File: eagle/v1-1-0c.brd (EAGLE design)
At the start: 313 x 132.9 mm, 179 parts, among them J1 CR22A-44D-2.54DSA(70), J3 26-60-4040, J4 AUDIO_JACK_3.5MM_PTH, J5 DIN5, SW1 3PDT-AQ-SWITCH, SW2 9077-1, U10 7805, U11 74LS10N, U13 74LS04N, U14 4528N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

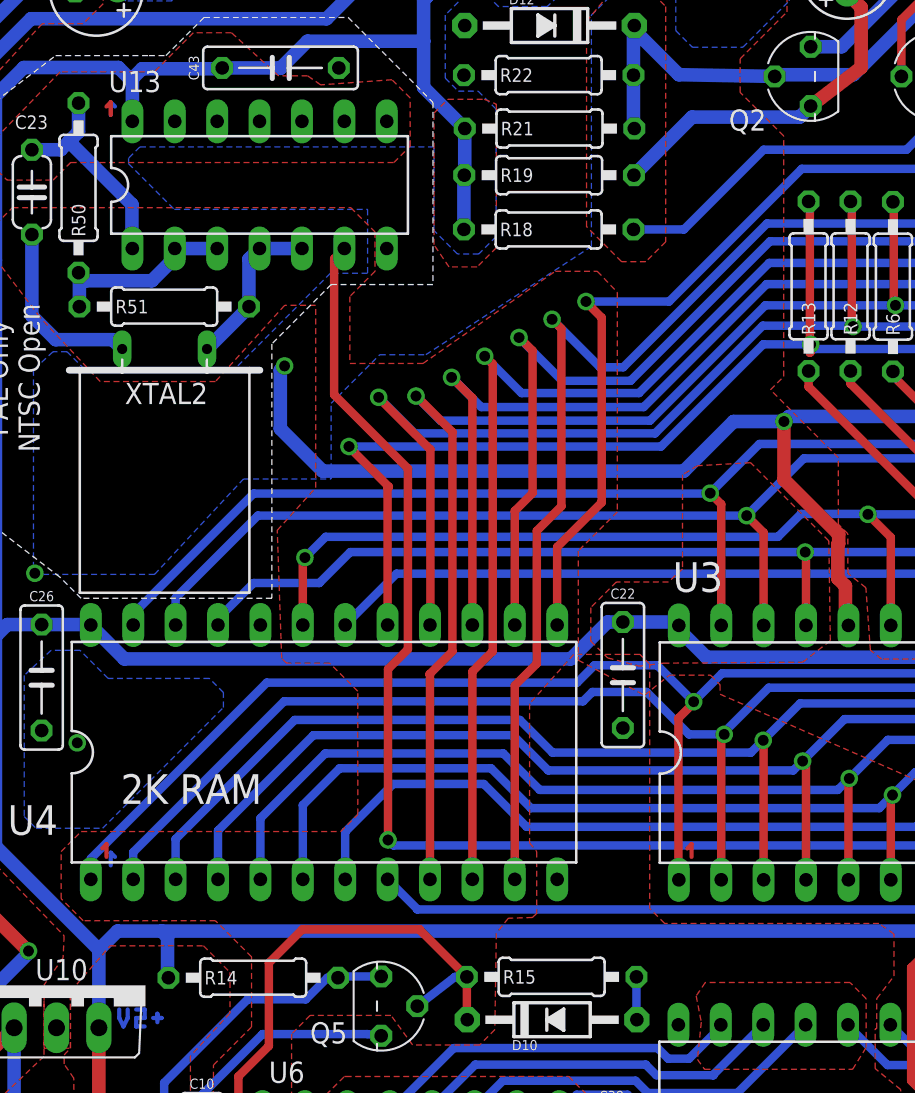
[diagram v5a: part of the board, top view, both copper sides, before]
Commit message: 19 OCT 2020 fixes from Errata
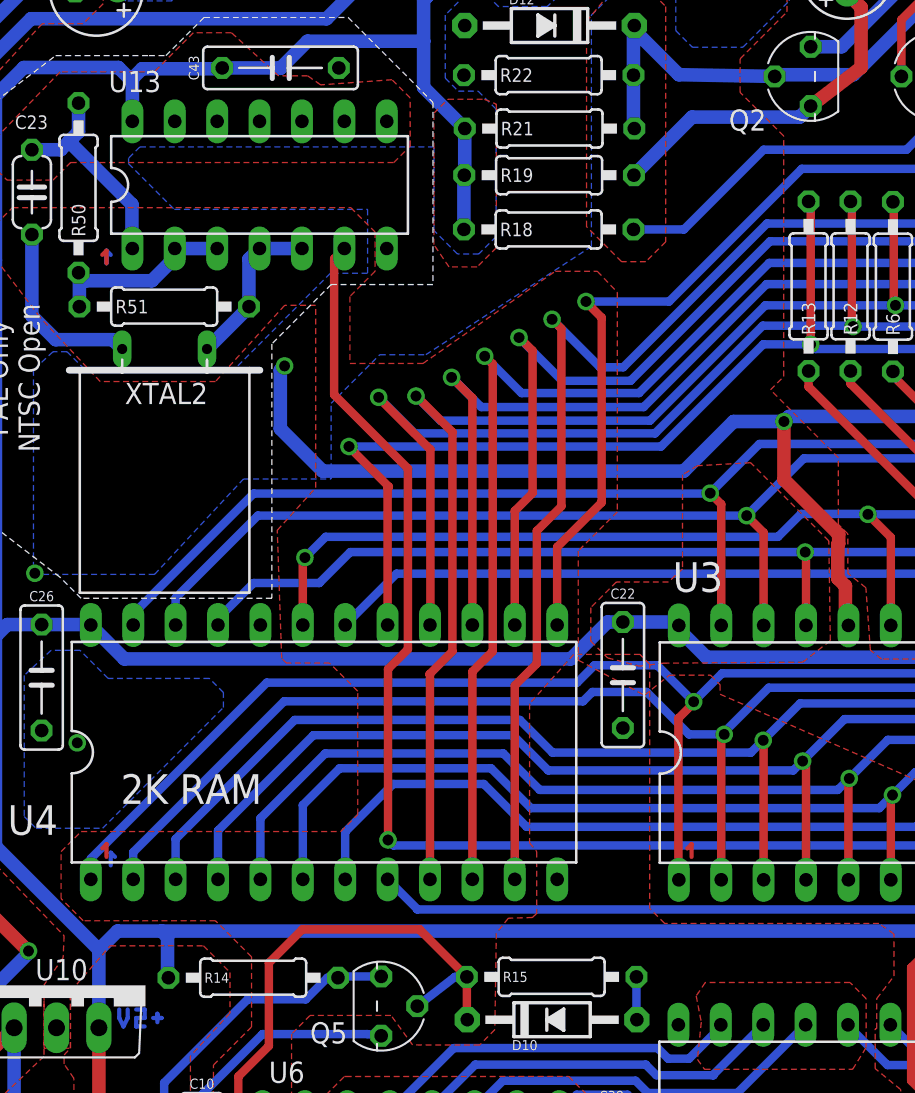
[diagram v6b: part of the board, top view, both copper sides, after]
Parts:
- C1: value 1uF @ 50v -> 1uF@50/10uF@16
- R14: value 2.2k -> 2.2k/680
- R15: value 1.2k -> 1.2k/2.2k
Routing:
- net CD07: track 106.2 -> 105.3 mm
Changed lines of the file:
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@@
 <grid distance="10" unitdist="mil" unit="mil" style="lines" multiple="1" display="no" altdistance="1" altunitdist="mil" altunit="mil"/>
 <layers>
-<layer number="1" name="Top" color="4" fill="1" visible="yes" active="yes"/>
+<layer number="1" name="Top" color="4" fill="1" visible="no" active="yes"/>
 <layer number="2" name="Route2" color="16" fill="1" visible="no" active="no"/>
 <layer number="3" name="Route3" color="17" fill="1" visible="no" active="no"/>
@@
 <layer number="14" name="Route14" color="22" fill="1" visible="no" active="no"/>
 <layer number="15" name="Route15" color="23" fill="1" visible="no" active="no"/>
-<layer number="16" name="Bottom" color="1" fill="1" visible="yes" active="yes"/>
+<layer number="16" name="Bottom" color="1" fill="1" visible="no" active="yes"/>
 <layer number="17" name="Pads" color="2" fill="1" visible="yes" active="yes"/>
 <layer number="18" name="Vias" color="2" fill="1" visible="yes" active="yes"/>
@@
 <layer number="46" name="Milling" color="3" fill="1" visible="yes" active="yes"/>
 <layer number="47" name="Measures" color="7" fill="1" visible="yes" active="yes"/>
-<layer number="48" name="Document" color="7" fill="1" visible="yes" active="yes"/>
+<layer number="48" name="Document" color="7" fill="1" visible="no" active="yes"/>
 <layer number="49" name="Reference" color="7" fill="1" visible="no" active="yes"/>
 <layer number="50" name="dxf" color="7" fill="1" visible="yes" active="yes"/>
@@
 <wire x1="9.599640625" y1="99.886" x2="11.58331875" y2="99.886" width="0.1524" layer="48"/>
 <wire x1="9.72361875" y1="89.49216875" x2="11.7073" y2="89.49216875" width="0.1524" layer="48"/>
-<wire x1="57.945209375" y1="75.54211875" x2="57.945209375" y2="62.39176875" width="0.1524" layer="48"/>
 <wire x1="56.9244" y1="74.606090625" x2="58.90808125" y2="74.606090625" width="0.1524" layer="48"/>
 <wire x1="57.04838125" y1="63.22148125" x2="59.032059375" y2="63.22148125" width="0.1524" layer="48"/>
@@
 <attribute name="VALUE" x="75.4888" y="72.1868" size="0.8128" layer="27" ratio="10" rot="R90" align="center-right"/>
 </element>
-<element name="R14" library="aq-rcl" package="0207/10" package3d_urn="urn:adsk.eagle:package:23491/2" value="2.2k" x="24.5364" y="27.813" smashed="yes">
-<attribute name="NAME" x="21.6154" y="27.813" size="0.8128" layer="25" ratio="10" align="center-left"/>
+<element name="R14" library="aq-rcl" package="0207/10" package3d_urn="urn:adsk.eagle:package:23491/2" value="2.2k/680" x="24.5364" y="27.813" smashed="yes">
+<attribute name="NAME" x="21.6154" y="27.813" size="0.6096" layer="25" ratio="10" align="center-left"/>
 <attribute name="POPULARITY" value="36" x="24.5364" y="27.813" size="1.778" layer="27" display="off"/>
 <attribute name="SPICEPREFIX" value="R" x="24.5364" y="27.813" size="1.778" layer="27" display="off"/>
-<attribute name="VALUE" x="27.4828" y="27.813" size="0.8128" layer="27" ratio="10" align="center-right"/>
+<attribute name="VALUE" x="27.4828" y="27.813" size="0.6096" layer="27" ratio="10" align="center-right"/>
 </element>
-<element name="R15" library="aq-rcl" package="0207/10" package3d_urn="urn:adsk.eagle:package:23491/2" value="1.2k" x="42.418" y="27.8638" smashed="yes">
-<attribute name="NAME" x="39.497" y="27.8638" size="0.8128" layer="25" ratio="10" align="center-left"/>
+<element name="R15" library="aq-rcl" package="0207/10" package3d_urn="urn:adsk.eagle:package:23491/2" value="1.2k/2.2k" x="42.418" y="27.8638" smashed="yes">
+<attribute name="NAME" x="39.497" y="27.8638" size="0.6096" layer="25" ratio="10" align="center-left"/>
 <attribute name="POPULARITY" value="36" x="42.418" y="27.8638" size="1.778" layer="27" display="off"/>
 <attribute name="SPICEPREFIX" value="R" x="42.418" y="27.8638" size="1.778" layer="27" display="off"/>
-<attribute name="VALUE" x="45.3644" y="27.8638" size="0.8128" layer="27" ratio="10" align="center-right"/>
+<attribute name="VALUE" x="45.3644" y="27.8638" size="0.6096" layer="27" ratio="10" align="center-right"/>
 </element>
 <element name="R55" library="aq-rcl" package="0207/10" package3d_urn="urn:adsk.eagle:package:23491/2" value="47k/∞" x="139.8524" y="12.319" smashed="yes">
@@
 <attribute name="VALUE" x="154.2542" y="6.8072" size="0.8128" layer="27" ratio="10"/>
 </element>
-<element name="C1" library="aq-rcl" package="E2,5-6" package3d_urn="urn:adsk.eagle:package:23349/1" value="1uF @ 50v" x="150.241" y="9.6266" smashed="yes" rot="R180">
+<element name="C1" library="aq-rcl" package="E2,5-6" package3d_urn="urn:adsk.eagle:package:23349/1" value="1uF@50/10uF@16" x="150.241" y="9.6266" smashed="yes" rot="R180">
 <attribute name="NAME" x="148.082" y="12.6746" size="0.8128" layer="25" ratio="10" rot="R180"/>
 <attribute name="POPULARITY" value="14" x="150.241" y="9.6266" size="1.778" layer="27" rot="R180" display="off"/>
 <attribute name="SPICEPREFIX" value="C" x="150.241" y="9.6266" size="1.778" layer="27" rot="R180" display="off"/>
-<attribute name="VALUE" x="147.574" y="5.7404" size="0.8128" layer="27" ratio="10"/>
+<attribute name="VALUE" x="150.368" y="5.7404" size="0.8128" layer="27" ratio="10" align="center"/>
 </element>
 <element name="C22" library="aq-rcl" package="C050-025X085" value=".1uF" x="46.6852" y="45.9486" smashed="yes" rot="R270">
@@
 <wire x1="48.9712" y1="59.6392" x2="55.0926" y2="65.7606" width="0.508" layer="16"/>
 <via x="57.9374" y="65.7606" extent="1-16" drill="0.65"/>
-<wire x1="57.9374" y1="65.7606" x2="57.9374" y2="65.3034" width="0.508" layer="1"/>
-<wire x1="57.8866" y1="65.2526" x2="57.9374" y2="65.3034" width="0.508" layer="1"/>
 <wire x1="57.9374" y1="65.7606" x2="55.0926" y2="65.7606" width="0.508" layer="16"/>
 <wire x1="79.1972" y1="65.4812" x2="58.2168" y2="65.4812" width="0.508" layer="16"/>
@@
 <contactref element="R13" pad="2"/>
 <wire x1="57.8104" y1="74.3204" x2="57.8866" y2="74.2442" width="0.508" layer="1"/>
-<wire x1="57.8866" y1="74.2442" x2="57.8866" y2="65.2526" width="0.508" layer="1"/>
 <contactref element="U4" pad="17"/>
 <wire x1="32.5882" y1="48.9458" x2="32.5882" y2="57.15" width="0.508" layer="1"/>
@@
 <wire x1="105.7656" y1="79.9338" x2="105.7656" y2="78.74" width="0.508" layer="16"/>
 <wire x1="105.7656" y1="78.74" x2="101.6508" y2="74.6252" width="0.508" layer="16"/>
+<wire x1="57.8104" y1="74.3204" x2="57.9374" y2="74.1934" width="0.508" layer="1"/>
+<wire x1="57.9374" y1="74.1934" x2="57.9374" y2="65.7606" width="0.508" layer="1"/>
 </signal>
 <signal name="CD06">
@@
 </signal>
 <signal name="N$23">
-<wire x1="15.748" y1="80.01" x2="16.002" y2="80.264" width="0.254" layer="1"/>
-<wire x1="16.002" y1="80.264" x2="16.002" y2="79.502" width="0.254" layer="1"/>
+<wire x1="15.494" y1="71.12" x2="15.748" y2="71.374" width="0.254" layer="1"/>
+<wire x1="15.748" y1="71.374" x2="15.748" y2="70.612" width="0.254" layer="1"/>
 </signal>
 <signal name="N$27">
@@
 </signal>
 <signal name="N$93">
-<wire x1="16.256" y1="80.01" x2="16.002" y2="80.264" width="0.254" layer="16"/>
-<wire x1="16.002" y1="80.264" x2="16.002" y2="79.502" width="0.254" layer="16"/>
+<wire x1="16.002" y1="71.12" x2="15.748" y2="71.374" width="0.254" layer="16"/>
+<wire x1="15.748" y1="71.374" x2="15.748" y2="70.612" width="0.254" layer="16"/>
 </signal>
 <signal name="N$94">

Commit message: Tweaks
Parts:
- C43: value ∞/0.1uF -> ∞/100nF
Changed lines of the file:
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@@
 <grid distance="10" unitdist="mil" unit="mil" style="lines" multiple="1" display="no" altdistance="1" altunitdist="mil" altunit="mil"/>
 <layers>
-<layer number="1" name="Top" color="4" fill="1" visible="no" active="yes"/>
+<layer number="1" name="Top" color="4" fill="1" visible="yes" active="yes"/>
 <layer number="2" name="Route2" color="16" fill="1" visible="no" active="no"/>
 <layer number="3" name="Route3" color="17" fill="1" visible="no" active="no"/>
@@
 <layer number="14" name="Route14" color="22" fill="1" visible="no" active="no"/>
 <layer number="15" name="Route15" color="23" fill="1" visible="no" active="no"/>
-<layer number="16" name="Bottom" color="1" fill="1" visible="no" active="yes"/>
+<layer number="16" name="Bottom" color="1" fill="1" visible="yes" active="yes"/>
 <layer number="17" name="Pads" color="2" fill="1" visible="yes" active="yes"/>
 <layer number="18" name="Vias" color="2" fill="1" visible="yes" active="yes"/>
@@
 <attribute name="VALUE" x="18.1864" y="74.676" size="1.27" layer="27" ratio="10"/>
 </element>
-<element name="C43" library="aq-rcl" package="C050-025X090" value="∞/0.1uF" x="26.2382" y="82.3214" smashed="yes">
+<element name="C43" library="aq-rcl" package="C050-025X090" value="∞/100nF" x="26.2382" y="82.3214" smashed="yes">
 <attribute name="NAME" x="21.2852" y="82.3214" size="0.6096" layer="25" ratio="10" rot="R90" align="bottom-center"/>
 <attribute name="VALUE" x="31.0642" y="82.3214" size="0.6096" layer="27" ratio="10" rot="R90" align="top-center"/>

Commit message: Clean up
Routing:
- net N$27: track 1.12 -> 2.24 mm
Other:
- board text added: "Aquarius Motherboard v1.1.0 Rev C - 21 OCT 2020 by Sean Harrington, sph@1stage.com"
- board text removed: "Aquarius Motherboard v1.1.0 Rev C - 18 OCT 2020 by Sean Harrington, sph@1stage.com"
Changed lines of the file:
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@@
 <layer number="46" name="Milling" color="3" fill="1" visible="yes" active="yes"/>
 <layer number="47" name="Measures" color="7" fill="1" visible="yes" active="yes"/>
-<layer number="48" name="Document" color="7" fill="1" visible="no" active="yes"/>
-<layer number="49" name="Reference" color="7" fill="1" visible="no" active="yes"/>
+<layer number="48" name="Document" color="7" fill="1" visible="yes" active="yes"/>
+<layer number="49" name="Reference" color="7" fill="1" visible="yes" active="yes"/>
 <layer number="50" name="dxf" color="7" fill="1" visible="yes" active="yes"/>
 <layer number="51" name="tDocu" color="7" fill="1" visible="yes" active="yes"/>
@@
 <text x="108.966" y="114.3" size="1.778" layer="21" align="center">RF Modulator</text>
 <text x="266.7" y="54.102" size="1.778" layer="21" align="center">Aquarius Motherboard v1.1.0
-Rev C - 18 OCT 2020
+Rev C - 21 OCT 2020
 by Sean Harrington, sph@1stage.com</text>
 <text x="44.2976" y="8.3058" size="0.8128" layer="21" rot="R180" align="center">This replaces
@@
 <wire x1="44.45" y1="9.906" x2="45.974" y2="11.6078" width="0.0762" layer="21"/>
 <wire x1="45.974" y1="11.6078" x2="45.974" y2="11.176" width="0.0762" layer="21"/>
-<frame x1="-11.176" y1="-13.462" x2="333.248" y2="144.78" columns="5" rows="3" layer="49"/>
 <text x="184.2262" y="87.6554" size="0.8128" layer="27">PAL 8.867238 Mhz</text>
 <text x="184.277" y="88.9762" size="0.762" layer="27">NTSC</text>
@@
 <wire x1="50.546" y1="35.56" x2="50.8" y2="35.814" width="0.254" layer="1"/>
 <wire x1="50.8" y1="35.814" x2="50.8" y2="35.052" width="0.254" layer="1"/>
+<wire x1="51.1048" y1="35.2044" x2="51.1048" y2="34.4424" width="0.254" layer="16"/>
+<wire x1="51.3588" y1="34.9504" x2="51.1048" y2="35.2044" width="0.254" layer="16"/>
+<wire x1="51.3588" y1="34.9504" x2="50.8" y2="35.052" width="0" layer="19" extent="1-16"/>
 </signal>
 <signal name="N$29">
